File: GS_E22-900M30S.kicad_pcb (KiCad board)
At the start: 2 copper layers, 60 x 60 mm, 11 parts, among them J1 Barrel_Jack, J3 Raspberry_Pi_2_3, U1 LT1085-5.0, U2 E22-900M30S

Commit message: Add files via upload
updated pcb
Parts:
- added G***: LOGO, LOGO, B.Cu at (97.5, 102.4)
- added H1: M, MountingHole:MountingHole_2.7mm_M2.5_Pad_Via, F.Cu at (82.0, 86.5)
- added H2: M, MountingHole:MountingHole_2.7mm_M2.5_Pad_Via, F.Cu at (140.0, 86.5)
- added H3: M, MountingHole:MountingHole_2.7mm_M2.5_Pad_Via, F.Cu at (82.0, 135.5)
- added H4: M, MountingHole:MountingHole_2.7mm_M2.5_Pad_Via, F.Cu at (140.0, 135.5)
- J3: moved to B.Cu
- R1: footprint Resistor_SMD:R_0603_1608Metric -> Resistor_SMD:R_0805_2012Metric_Pad1.20x1.40mm_HandSolder
- moved C4 43.4 mm to (131.3, 131.4), turned to 0 degrees
- moved R1 40.5 mm to (139.4, 102.6), turned to -90 degrees
- moved J1 38.4 mm to (92.3, 123.9), turned to 90 degrees
- moved R2 38.1 mm to (123.8, 131.4), turned to 90 degrees
- moved U1 37.5 mm to (110.9, 133.0), turned to 90 degrees
- moved C3 37.4 mm to (131.3, 125.9), turned to 0 degrees
- moved C1 36.5 mm to (103.8, 130.6), turned to -90 degrees
- moved C2 32.8 mm to (117.3, 129.4), turned to -90 degrees
- moved D1 31.7 mm to (123.8, 126.4), turned to -90 degrees
- moved J3 12.1 mm to (86.9, 87.8), turned to -90 degrees
- moved U2 6.33 mm to (117.3, 108.4), turned to -90 degrees
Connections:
- R1 pad 1: RF_RESET -> GND
- R1 pad 2: GND -> RF_RESET
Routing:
- net GND: track 237.9 -> 3.40 mm, vias 4 -> 1
- net RF_DIO1: track 74.5 -> 12.1 mm, vias 2 -> 0
- net RF_RESET: track 81.1 -> 30.0 mm
- net RF_BUSY: track 37.4 -> 9.47 mm, vias 2 -> 0
- net RF_DIO2: track 71.7 -> 52.6 mm
- net RF_RXEN: track 73.9 -> 58.5 mm, vias 2 -> 0
- net RF_MOSI: track 10.2 -> 19.5 mm, vias 0 -> 1
- net RF_TXEN: track 64.2 -> 55.1 mm, vias 1 -> 0
- net RF_MISO: track 14.8 -> 20.0 mm, vias 2 -> 1
- net RF_SCK: track 12.4 -> 10.6 mm
- net RF_CS: track 13.7 -> 13.1 mm
- added copper zone on B.Cu, net GND
- added copper zone on F.Cu, net GND
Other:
- board size 60 x 60 mm -> 65 x 56 mm
- board text added: "Argus-2 Ground Station"
- board text added: "Carnegie Mellon University"

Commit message: Add files via upload
updated PCB hopefully final
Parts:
- G***: moved to F.Cu
- moved G*** 9.72 mm to (88.0, 100.9), turned to 0 degrees
- moved C4 6.15 mm to (134.9, 126.5), turned to -90 degrees
- moved C3 1.93 mm to (129.4, 126.5), turned to -90 degrees
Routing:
- net VCC: track 24.6 -> 5.09 mm, vias 0 -> 1
- net RF_RXEN: track 58.5 -> 46.7 mm
- net V_RF: track 42.3 -> 33.4 mm, vias 0 -> 2
- net RF_TXEN: track 55.1 -> 47.9 mm
- net GND: vias 1 -> 0
- added copper zone on B.Cu, net VCC
- added copper zone on B.Cu, net V_RF
- removed copper zone on B.Cu, net GND
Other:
- board text added: "Ground Station"
- board text removed: "Argus-2 Ground Station"
- board text removed: "Carnegie Mellon University"

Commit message: Add files via upload
Final schematic and PCB board
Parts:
- removed G***: LOGO, LOGO
- added J2: V_RF, MountingHole:MountingHole_2.2mm_M2_DIN965_Pad, F.Cu at (83.7, 107.3)
- added J4: GND, MountingHole:MountingHole_2.2mm_M2_DIN965_Pad, F.Cu at (83.7, 112.7)
- added J5: VCC, MountingHole:MountingHole_2.2mm_M2_DIN965_Pad, F.Cu at (83.7, 118.0)
- moved C1 0.69 mm to (103.9, 129.9)
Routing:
- net V_RF: track 33.4 -> 56.5 mm, vias 2 -> 1
- net RF_RXEN: track 46.7 -> 57.5 mm, vias 0 -> 1
- net RF_TXEN: track 47.9 -> 58.7 mm, vias 0 -> 1
- net VCC: track 5.09 -> 12.5 mm, vias 1 -> 0
- net GND: track 3.40 -> 1.68 mm, vias 0 -> 47
- net RF_DIO2: track 52.6 -> 51.1 mm
- added copper zone on B.Cu, net GND
- added copper zone on F.Cu, net VCC
- added copper zone on F.Cu, net V_RF
- removed copper zone on B.Cu, net VCC
- removed copper zone on B.Cu, net V_RF
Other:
- board text added: "+"
- board text added: "Argus-2 Groundstation v1"
- board text added: "CMU Spacecraft - Fall - 2024"
- board text added: "Carnegie Mellon Argus - 2 Ground Station"
- board text added: "Commarades Designer: Shashwat Singh"
- board text added: "GND"
- board text added: "VCC"
- board text added: "V_RF"
- board text removed: "Ground Station"

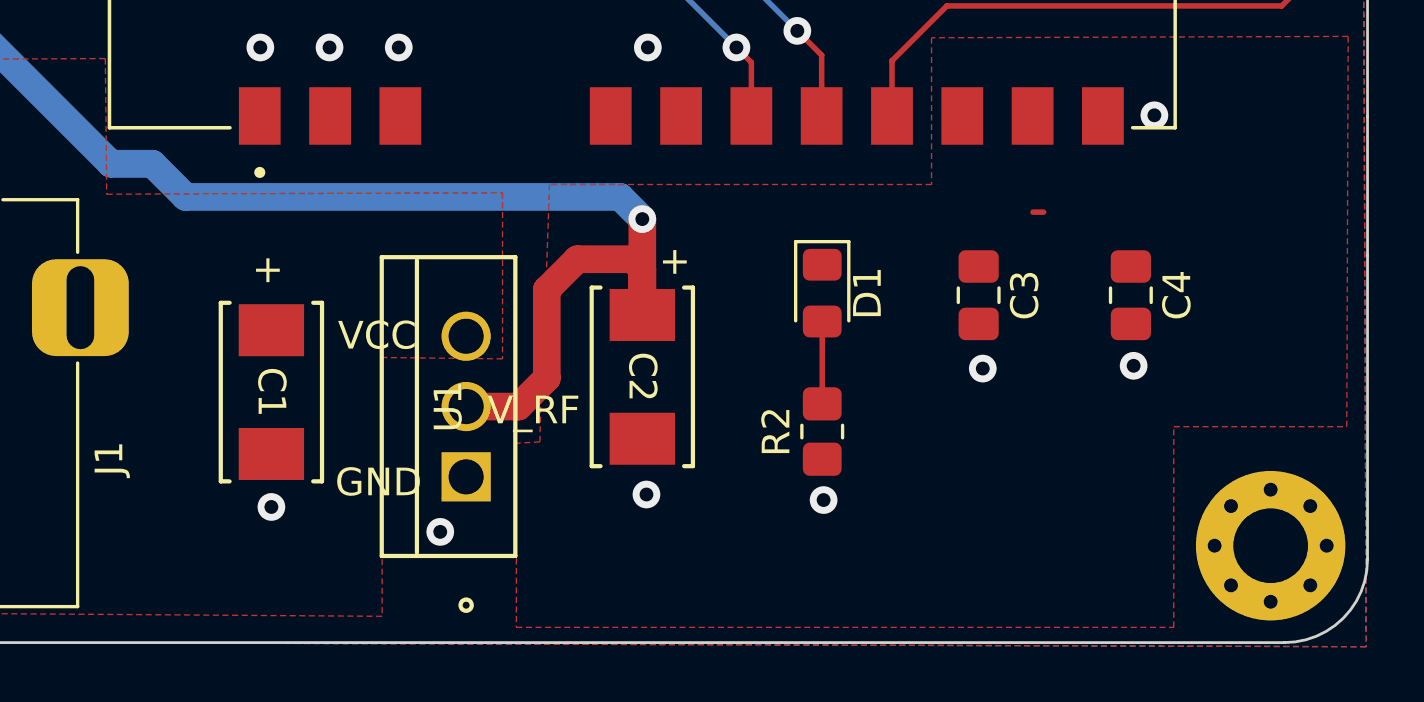
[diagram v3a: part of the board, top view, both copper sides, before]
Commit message: Add files via upload
Hopefully this is the final version with the SMT voltage regulator with the new schematic as well.
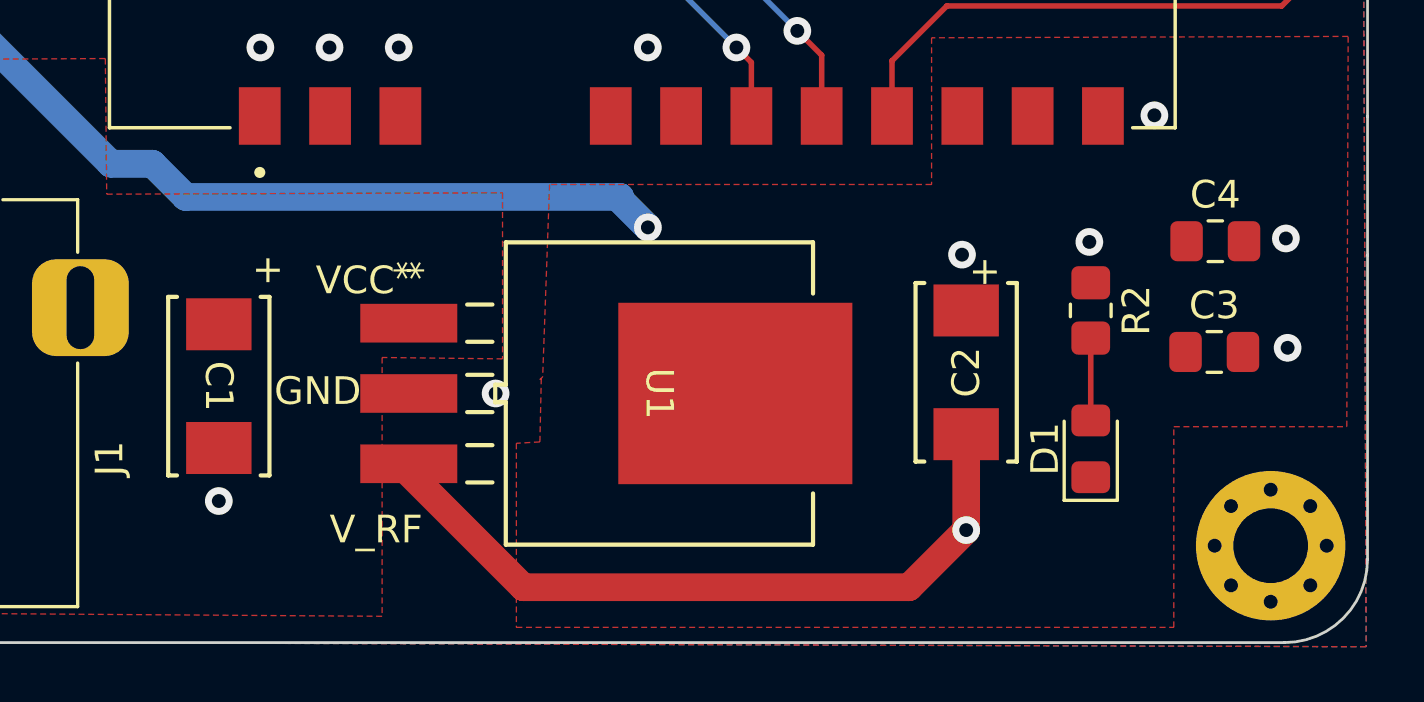
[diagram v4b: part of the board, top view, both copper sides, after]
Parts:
- C2: value 22uF -> 10uF
- U1: value LT1085-5.0 -> MIC29300-5.0WU-TR; footprint LT1085-5:TO220-3_T_LIT -> MIC29300_5:TO-263-3_MCH
- moved C2 11.7 mm to (129.0, 129.2), turned to 90 degrees
- moved D1 11.2 mm to (133.5, 132.0), turned to 90 degrees
- moved R2 10.6 mm to (133.5, 127.0), turned to -90 degrees
- moved C3 8.76 mm to (138.0, 128.5), turned to 0 degrees
- moved U1 7.60 mm to (117.9, 130.0), turned to -90 degrees
- moved C4 3.62 mm to (138.0, 124.5), turned to 0 degrees
- moved C1 1.91 mm to (102.0, 129.7)
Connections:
- U1 pad 1: GND -> VCC
- U1 pad 2: V_RF -> GND
- U1 pad 3: VCC -> V_RF
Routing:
- net V_RF: track 56.5 -> 67.3 mm, vias 1 -> 2
- net GND: track 1.68 -> 0.57 mm

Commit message: Add files via upload
final update
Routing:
- net V_RF: vias 2 -> 1
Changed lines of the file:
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@@
 		(tags "capacitor handsolder")
 		(property "Reference" "C4"
-			(at 0 -1.68 360)
+			(at 0 -1.68 0)
 			(layer "F.SilkS")
 			(effects
@@
 		)
 		(property "Value" "10uF"
-			(at 0 1.68 360)
+			(at 0 1.68 0)
 			(layer "F.Fab")
 			(effects
@@
 		)
 		(fp_text user "${REFERENCE}"
-			(at 0 0 360)
+			(at 0 0 0)
 			(layer "F.Fab")
 			(effects
@@
 		(tags "capacitor handsolder")
 		(property "Reference" "C3"
-			(at 0 -1.68 360)
+			(at 0 -1.68 0)
 			(layer "F.SilkS")
 			(effects
@@
 		)
 		(property "Value" "100nF"
-			(at 0 1.68 360)
+			(at 0 1.68 0)
 			(layer "F.Fab")
 			(effects
@@
 		)
 		(fp_text user "${REFERENCE}"
-			(at 0 0 360)
+			(at 0 0 0)
 			(layer "F.Fab")
 			(effects
@@
 		(size 1)
 		(drill 0.5)
-		(layers "F.Cu" "B.Cu")
-		(net 2)
-	)
-	(via
-		(at 129 134.9352)
-		(size 1)
-		(drill 0.5)
